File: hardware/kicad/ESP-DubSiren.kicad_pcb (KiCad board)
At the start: 2 copper layers, 15.6 x 2.1 mm, 68 parts, among them J1 USB4085-GF-A, J2 RCJ-2123, SW1 MX2A-11NW, SW2 MX2A-11NW, SW3 MX2A-11NW, SW4 MX2A-11NW, SW5 RESET, SW6 BOOT, SW7 PEC11R-4120F-S0018, U1 ESP32-S3-WROOM-1U-N16R8, U2 MPM3612GLQ-33-Z, U3 74HC4051D, U4 USBLC6-2SC6, U5 Adafruit 5393, U6 Adafruit 6250, U7 TPS22918DBVR

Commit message: Replace RCA with NRJ4HF and document rear mechanical study
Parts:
- J2: value RCJ-2123 -> NRJ4HF; footprint ESP-DubSiren-V2-Mechanical:SameSky_RCJ-2123 -> Connector_Audio:Jack_6.35mm_Neutrik_NRJ4HF_Horizontal
- moved J2 10.1 mm to (86.7, 20.3), turned to 90 degrees

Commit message: Review electrical design and propose standalone PCB layout (#34, #35)
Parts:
- moved SW6 70.2 mm to (81.0, 86.0)
- moved SW5 70.0 mm to (81.0, 70.0)
- moved U6 63.4 mm to (13.0, 55.5), turned to 90 degrees
- moved H4 34.5 mm to (81.0, 115.0)
- moved H2 32.8 mm to (81.0, 5.00)
- moved SW4 30.8 mm to (78.5, 94.9)
- moved RV6 30.5 mm to (71.0, 79.0)
- moved SW3 29.9 mm to (56.5, 94.9)
- moved SW2 28.9 mm to (34.5, 94.9)
- moved SW1 28.1 mm to (12.5, 94.9)
- moved R13 27.2 mm to (76.0, 93.0)
- moved TP3 26.9 mm to (5.00, 110.0)
- moved RV3 26.6 mm to (71.0, 24.0)
- moved RV5 24.6 mm to (43.0, 79.0)
- moved SW7 23.7 mm to (75.0, 52.5)
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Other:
- board size 15.6 x 2.1 mm -> 86 x 120 mm
- board text added: "86 x 120 mm / R3 / M3 D3.2"
- board text added: "H1-H4: KEEP FREE 8x8 mm BOTH SIDES"
- board text added: "KEYCAP 20x20: UNVERIFIED"

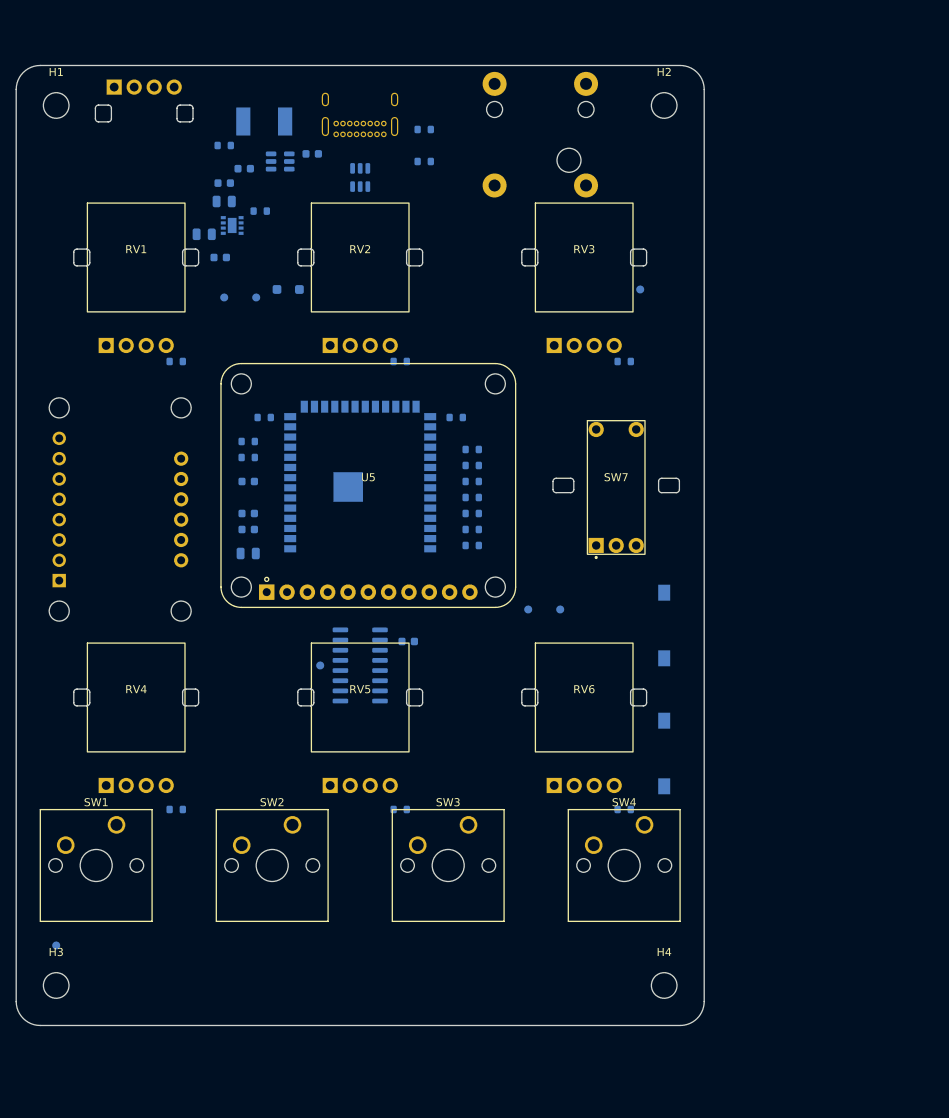
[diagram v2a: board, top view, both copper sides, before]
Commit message: Increase control clearances on 86x126 standalone PCB
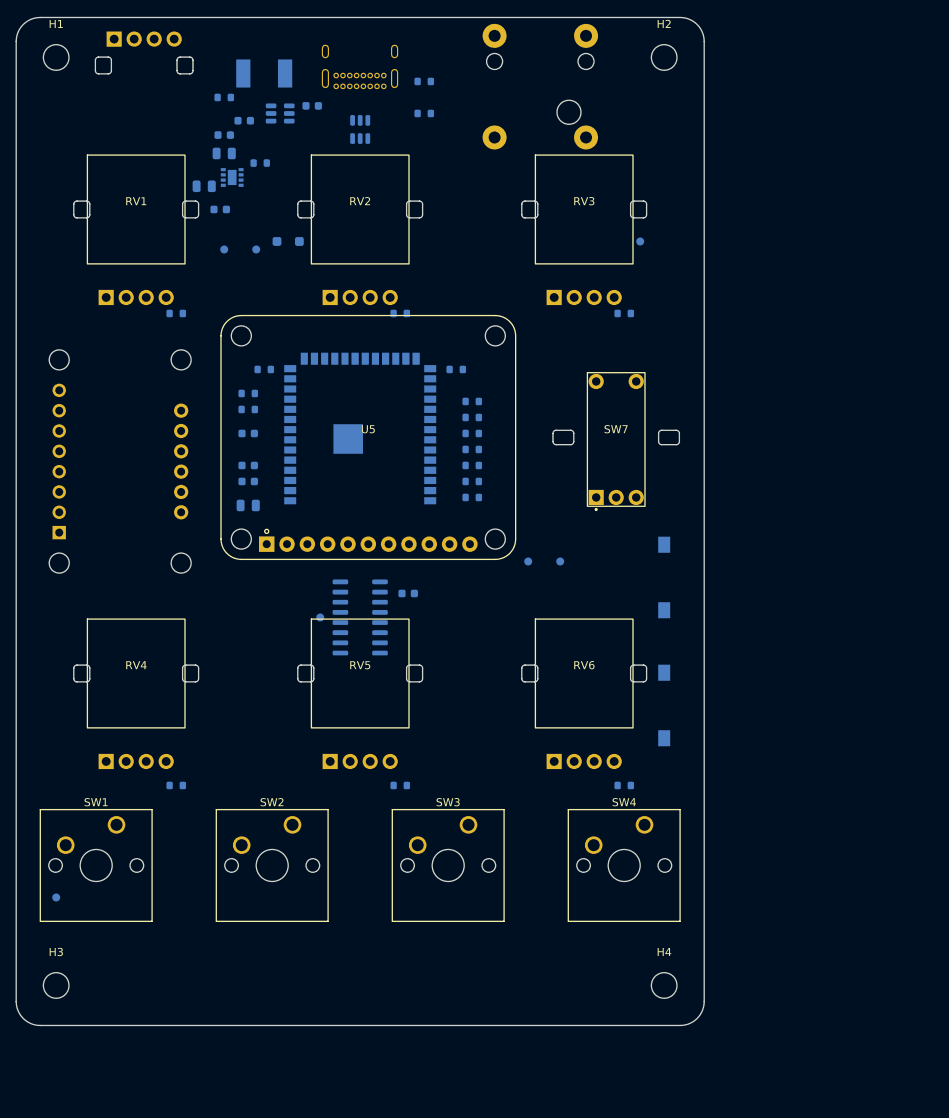
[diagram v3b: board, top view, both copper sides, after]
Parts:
- moved C1 6.00 mm to (23.5, 15.1)
- moved C11 6.00 mm to (37.0, 5.05)
- moved C10 6.00 mm to (28.5, 6.90)
- moved C2 6.00 mm to (25.5, 18.0)
- moved C3 6.00 mm to (26.0, 11.0)
- moved C4 6.00 mm to (26.0, 8.70)
- moved C5 6.00 mm to (29.0, 55.0)
- moved C6 6.00 mm to (29.0, 50.0)
- moved C7 6.00 mm to (29.0, 46.0)
- moved C8 6.00 mm to (49.0, 66.0)
- moved C9 6.00 mm to (29.0, 52.0)
- moved D1 6.00 mm to (34.0, 22.0)
- moved F1 6.00 mm to (31.0, 1.00)
- moved H1 6.00 mm to (5.00, -1.00)
- moved H2 6.00 mm to (81.0, -1.00)
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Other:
- board size 86 x 120 mm -> 86 x 126 mm
- board text added: "GAPS: KEYS 4.08 / DISPLAY 4.34 mm NOMINAL"
- board text added: "M3 RESERVE 8x8 BOTH SIDES - NO ROUTING"
- board text added: "STANDALONE 86x126 R3 - M3 3.2"
- board text removed: "86 x 120 mm / R3 / M3 D3.2"
- board text removed: "H1-H4: KEEP FREE 8x8 mm BOTH SIDES"
- board text removed: "KEYCAP 20x20: UNVERIFIED"

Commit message: Add issue 36 front silkscreen, assembly guide and review previews
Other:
- board text added: "BTN1"
- board text added: "BTN2"
- board text added: "BTN3"
- board text added: "BTN4"
- board text added: "ECHO CUT"
- board text added: "ECHO FEEDBACK"
- board text added: "ECHO FILTER"
- board text added: "ECHO LEVEL"
- board text added: "ECHO TIME"
- board text added: "ESP-DubSiren"
- board text added: "HOLD"
- board text added: "MANUAL MOD"
- board text added: "MASTER"
- board text added: "MONO"
- board text added: "PITCH"
- board text added: "PUSH: MENU"
- board text added: "RATE"
- board text added: "SELECT"
- board text added: "TRIGGER"
- board text added: "USB-C"

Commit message: Preserve accepted issue 36 silkscreen cleanup and local corrections
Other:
- board text removed: "BTN1"
- board text removed: "BTN2"
- board text removed: "BTN3"
- board text removed: "BTN4"
- board text removed: "ECHO CUT"
- board text removed: "ECHO FEEDBACK"
- board text removed: "ECHO FILTER"
- board text removed: "ECHO LEVEL"
- board text removed: "ECHO TIME"
- board text removed: "ESP-DubSiren"
- board text removed: "GAPS: KEYS 4.08 / DISPLAY 4.34 mm NOMINAL"
- board text removed: "HOLD"
- board text removed: "M3 RESERVE 8x8 BOTH SIDES - NO ROUTING"
- board text removed: "MANUAL MOD"
- board text removed: "MONO"
- board text removed: "PITCH"
- board text removed: "PUSH: MENU"
- board text removed: "RATE"
- board text removed: "SELECT"
- board text removed: "STANDALONE 86x126 R3 - M3 3.2"
- board text removed: "TRIGGER"
- board text removed: "USB-C"

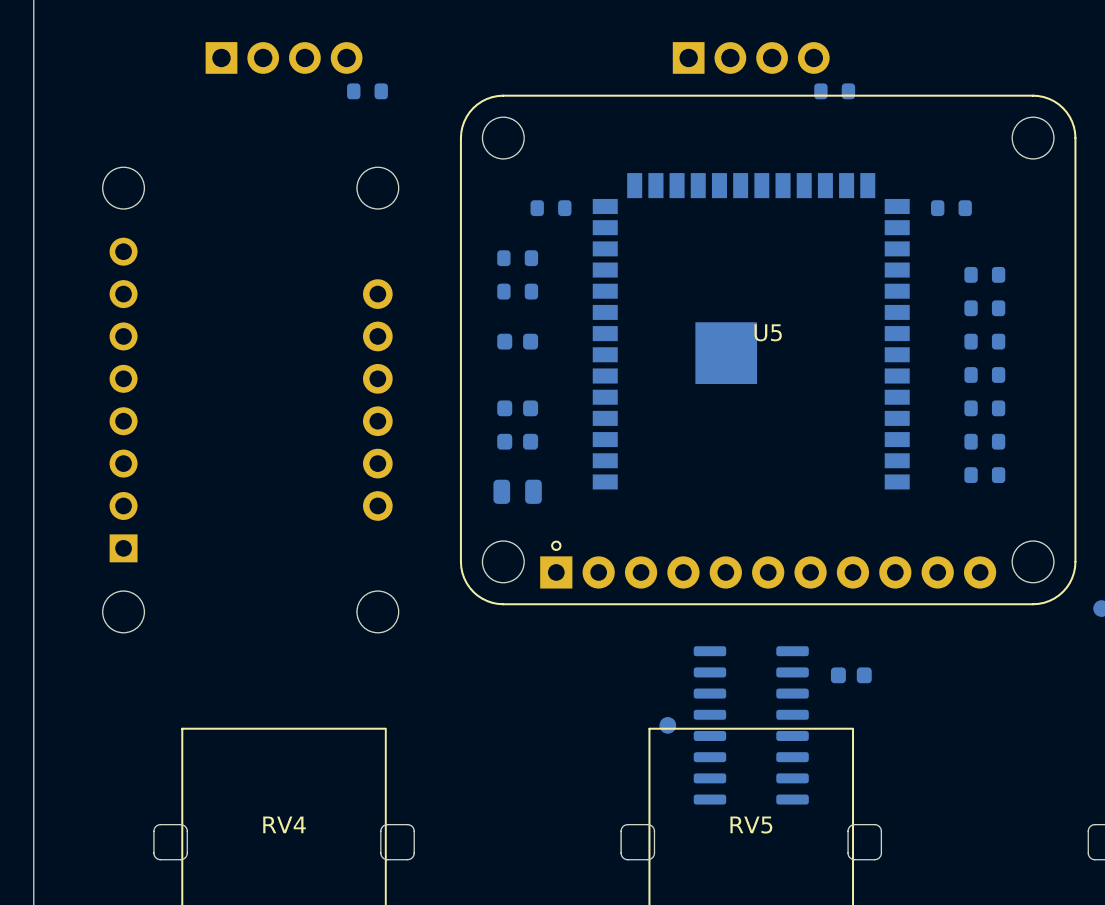
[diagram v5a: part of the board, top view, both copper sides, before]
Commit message: Study issue 38 rear placement with DAC under display
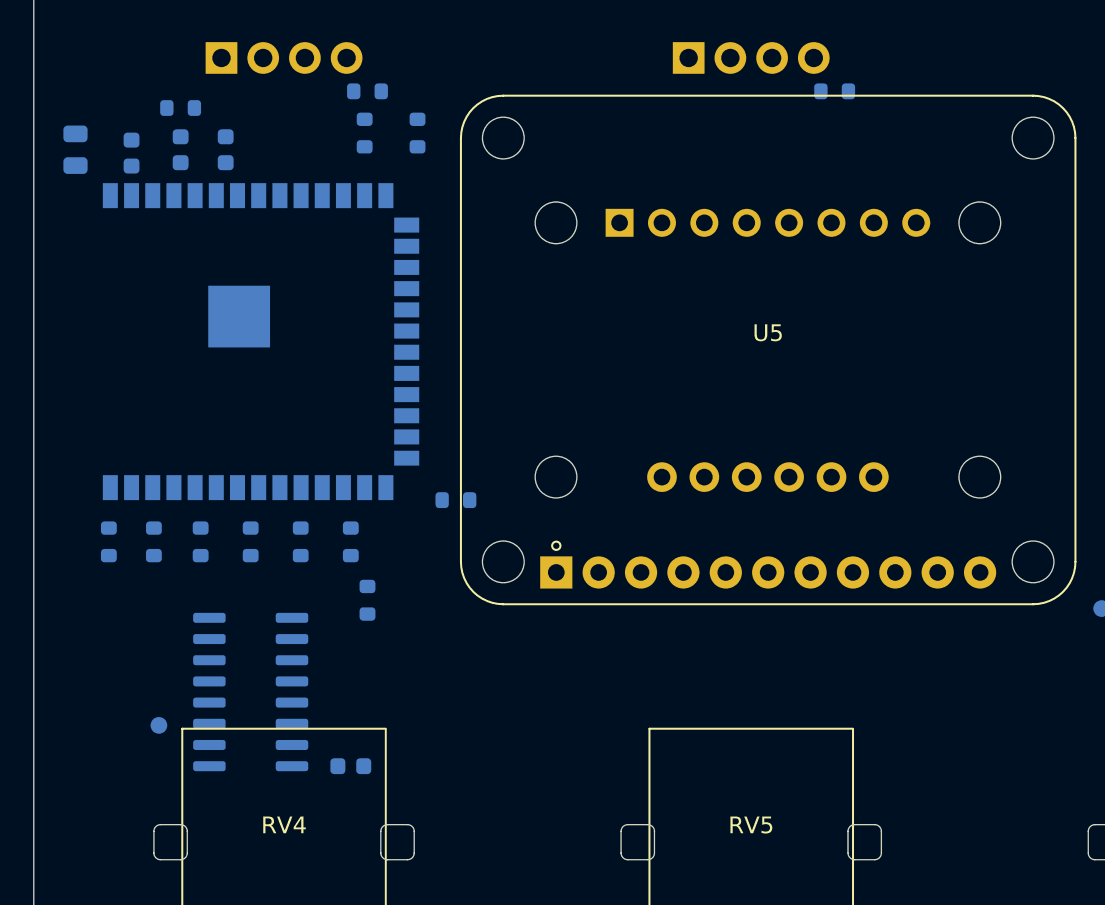
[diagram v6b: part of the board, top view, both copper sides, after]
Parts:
- moved R19 53.1 mm to (4.50, 58.0), turned to 90 degrees
- moved R20 50.2 mm to (7.20, 58.0), turned to 90 degrees
- moved R18 48.1 mm to (10.0, 58.0), turned to 90 degrees
- moved R17 45.6 mm to (13.0, 58.0), turned to 90 degrees
- moved R16 43.3 mm to (16.0, 58.0), turned to 90 degrees
- moved R15 41.2 mm to (19.0, 58.0), turned to 90 degrees
- moved R21 37.8 mm to (20.0, 61.5), turned to 90 degrees
- moved R7 34.5 mm to (25.3, 55.5)
- moved C5 33.5 mm to (2.50, 34.5), turned to 90 degrees
- moved U6 31.1 mm to (44.0, 46.5), turned to 0 degrees
- moved TP4 30.5 mm to (7.50, 69.0)
- moved C8 30.5 mm to (19.0, 71.4)
- moved U3 30.1 mm to (13.0, 67.0)
- moved U1 30.0 mm to (13.0, 46.0), turned to -90 degrees
- moved C6 27.7 mm to (5.86, 34.7), turned to 90 degrees
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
